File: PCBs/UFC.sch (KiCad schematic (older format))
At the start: 33 parts, among them J1 8 Pin Connector, SW1 SW_SPST, SW10 SW_SPST, SW11 SW_SPST, SW12 SW_SPST, SW13 SW_SPST, SW14 SW_SPST, SW15 SW_SPST, SW16 SW_SPST, SW17 SW_SPST, SW2 SW_SPST, SW3 SW_SPST, SW4 SW_SPST, SW5 SW_SPST, SW6 SW_SPST, SW7 SW_SPST, SW8 SW_SPST, SW9 SW_SPST, U1 STM32F103C8T6

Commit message: Split up board, started routing traces
Moved the LED drivers and the STM32 board off of the main board and onto a daughterboard to fit a reasonable space. Second board will go behind the first, connected with .1" headers. 
Additionally, traces on the bottom four (second LED driver) OPT displays are routed. 
Redid the OPT buttons to be included in the keypad matrix, to save pins.
Removed the shift register pins and wired it all directly to the STM32, to save space
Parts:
- removed A1: ShiftRegisterBoard, UFC:ShiftRegisterBoardPins, symbol UFClib:ShiftRegisterBoard
- removed C3: .1nF, Capacitor_SMD:C_0603_1608Metric_Pad1.08x0.95mm_HandSolder, symbol Device:C
- removed J1: 8 Pin Connector, UFC:8pin254mm, symbol Connector_Generic_MountingPin:Conn_01x08_MountingPin
- removed U1: STM32F103C8T6, UFC:Bluepill, symbol UFClib:STM32F103C8T6
- added D13, D14, D15, D16, D17: D, Keypad:1N4148, symbol Device:D
- added D18, D19, D20, D21, D22, D23, D24, D25, D26, D27, D28, D29, D30, D31, D32, D33, D34: LED, LED_SMD:LED_0805_2012Metric_Pad1.15x1.40mm_HandSolder, symbol Device:LED
- added DS1: Scratchpad, UFC:Scratchpad, symbol UFClib:Scratchpad
- added DS2, DS3, DS4, DS5, DS6: CustomOptPanel, UFC:OPTDisplay, symbol UFClib:CustomOptPanel
- added DS7, DS8: 14SegDisplayLumex, UFC:LDS-F3902RI, symbol UFClib:14SegDisplayLumex
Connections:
- net labels added: A1, A2, B1, B2, C1, C2, COL4, COM0-1, COM0-2, COM1-1, COM1-2, COM10-1, COM10-2, COM11-1, COM11-2, COM12-1, COM12-2, COM13-1, COM13-2, COM14-1, COM14-2, COM15-1, COM15-2, COM2-1, COM2-2, COM3-1, COM3-2, COM4-1, COM4-2, COM5-1, COM5-2, COM6-1, COM6-2, COM7-1, COM7-2, COM8-1, COM8-2, COM9-1, COM9-2, D1, D2, DOT1, DOT2, DP1, DP2, E1, E2, F1, F2, G1, G2, H1, H2, J1, J2, K1, K2, L1, L2, LEDPWM, M1, M2, N1, N2, P1, P2, Q1, Q2, ROW0
- net labels removed: CS1, CS2, DATA, RD, SRCLK, SRCS, SRMISO, SW13, SW14, SW15, SW16, SW17, WR
- wire segments 62 -> 313
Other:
- note added: "COM Channel Displays\n"
- note added: "DIG0-3 controls the halves of the two 16 segment digits\nDIG4-8 controls the 7 segment digits, 2 digits per common pin"
- note added: "Keypad LEDs\n"
- note added: "OPT button LEDs\n"
- moved on the sheet: D1, D10, D11, D12, D2, D3, D4, D5, D6, D7, D8, D9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

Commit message: Finished routing, updated comm channel displays
Decided to use (and again modify) open hornet's com channel indicators. Finished routing traces and adding ground planes on the main board, though it may be a little sloppy. Began work on the back side board, which will have the LED drivers and STM32. Re added the shift register board for now for the sake of having more pins.
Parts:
- removed DS7, DS8: 14SegDisplayLumex, UFC:LDS-F3902RI, symbol UFClib:14SegDisplayLumex
- added DS7, DS8: CommDS, UFC:OHComm, symbol UFClib:CommDS
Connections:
- wire segments 313 -> 311
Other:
- moved on the sheet: D1, D10, D11, D12, D13, D14, D15, D16, D17, D18, D19, D2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

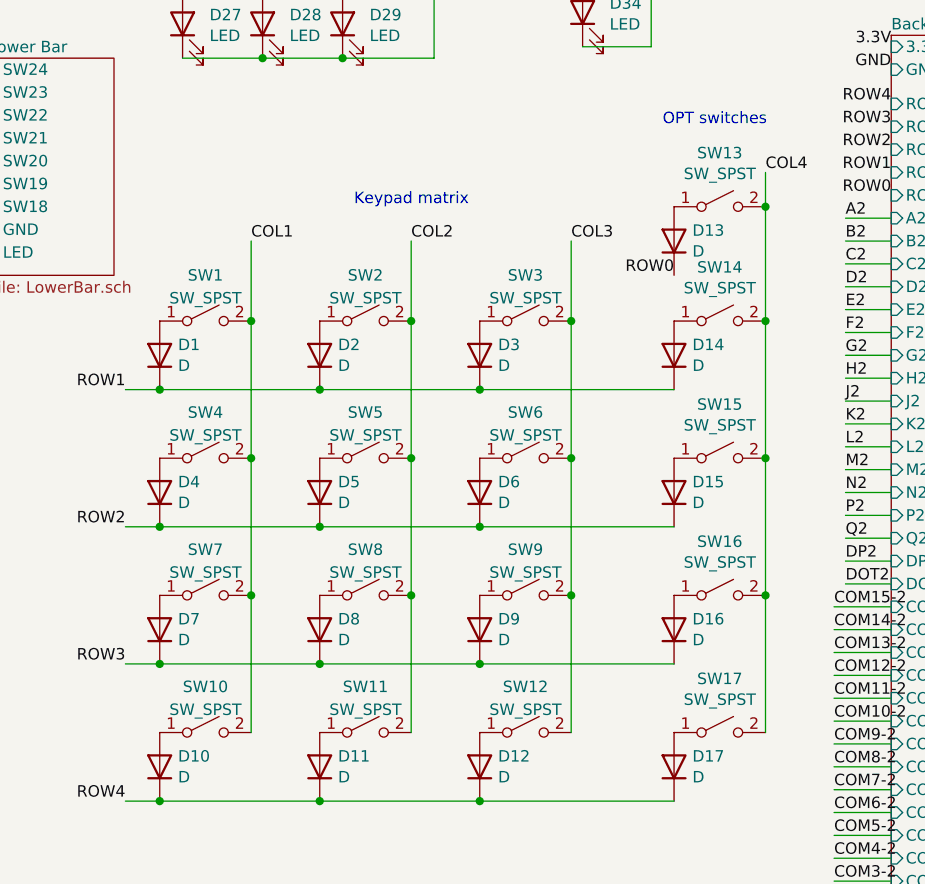
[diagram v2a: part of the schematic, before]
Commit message: Updated silkscreen, fixed minor issues
Updated silkscreen to include pin designations, and fixed minor issue with ground plane
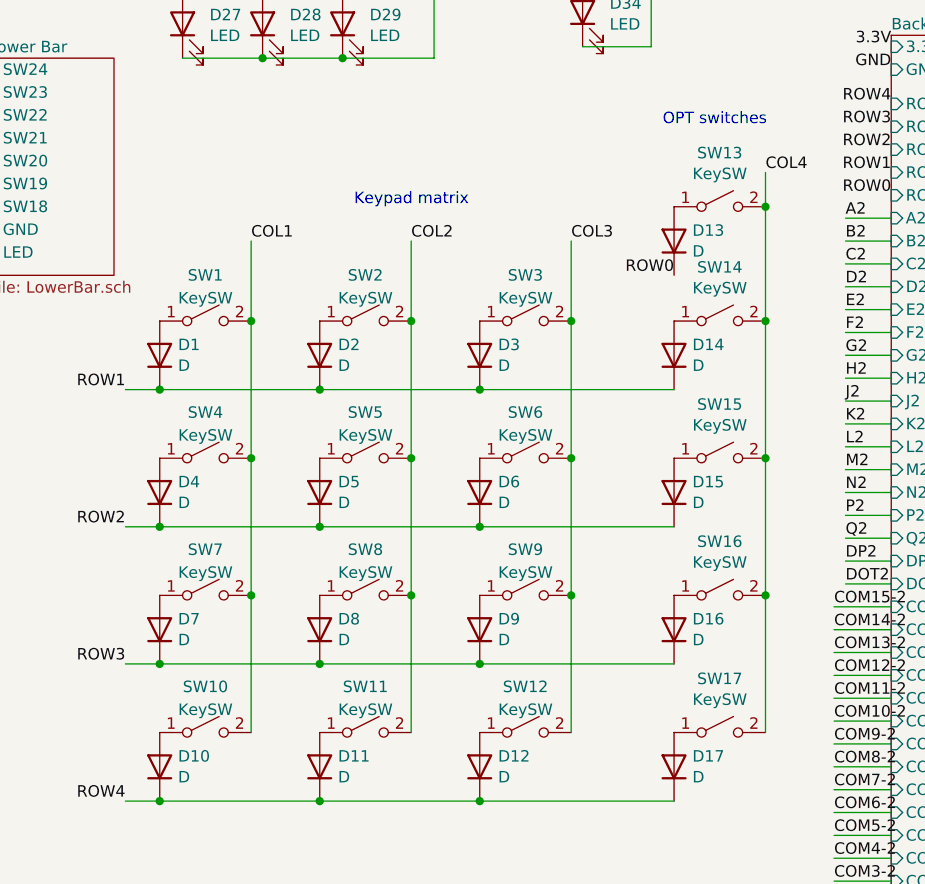
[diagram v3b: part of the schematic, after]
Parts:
- SW1, SW10, SW11, SW12, SW13, SW14, SW15, SW16, SW17, SW2, SW3, SW4, SW5, SW6, SW7, SW8, SW9: value SW_SPST -> KeySW
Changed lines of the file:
@@
 P 2200 4000
 F 0 "SW1" H 2200 4200 50  0000 C CNN
-F 1 "SW_SPST" H 2200 4100 50  0000 C CNN
+F 1 "KeySW" H 2200 4100 50  0000 C CNN
 F 2 "Keypad:KailhSW" H 2200 4000 50  0001 C CNN
 F 3 "~" H 2200 4000 50  0001 C CNN
@@
 P 2900 4000
 F 0 "SW2" H 2900 4200 50  0000 C CNN
-F 1 "SW_SPST" H 2900 4100 50  0000 C CNN
+F 1 "KeySW" H 2900 4100 50  0000 C CNN
 F 2 "Keypad:KailhSW" H 2900 4000 50  0001 C CNN
 F 3 "~" H 2900 4000 50  0001 C CNN
@@
 P 3600 4000
 F 0 "SW3" H 3600 4200 50  0000 C CNN
-F 1 "SW_SPST" H 3600 4100 50  0000 C CNN
+F 1 "KeySW" H 3600 4100 50  0000 C CNN
 F 2 "Keypad:KailhSW" H 3600 4000 50  0001 C CNN
 F 3 "~" H 3600 4000 50  0001 C CNN
@@
 P 2200 4600
 F 0 "SW4" H 2200 4800 50  0000 C CNN
-F 1 "SW_SPST" H 2200 4700 50  0000 C CNN
+F 1 "KeySW" H 2200 4700 50  0000 C CNN
 F 2 "Keypad:KailhSW" H 2200 4600 50  0001 C CNN
 F 3 "~" H 2200 4600 50  0001 C CNN
@@
 P 2900 4600
 F 0 "SW5" H 2900 4800 50  0000 C CNN
-F 1 "SW_SPST" H 2900 4700 50  0000 C CNN
+F 1 "KeySW" H 2900 4700 50  0000 C CNN
 F 2 "Keypad:KailhSW" H 2900 4600 50  0001 C CNN
 F 3 "~" H 2900 4600 50  0001 C CNN
@@
 P 3600 4600
 F 0 "SW6" H 3600 4800 50  0000 C CNN
-F 1 "SW_SPST" H 3600 4700 50  0000 C CNN
+F 1 "KeySW" H 3600 4700 50  0000 C CNN
 F 2 "Keypad:KailhSW" H 3600 4600 50  0001 C CNN
 F 3 "~" H 3600 4600 50  0001 C CNN
@@
 P 2200 5800
 F 0 "SW10" H 2200 6000 50  0000 C CNN
-F 1 "SW_SPST" H 2200 5900 50  0000 C CNN
+F 1 "KeySW" H 2200 5900 50  0000 C CNN
 F 2 "Keypad:KailhSW" H 2200 5800 50  0001 C CNN
 F 3 "~" H 2200 5800 50  0001 C CNN
@@
 P 2900 5800
 F 0 "SW11" H 2900 6000 50  0000 C CNN
-F 1 "SW_SPST" H 2900 5900 50  0000 C CNN
+F 1 "KeySW" H 2900 5900 50  0000 C CNN
 F 2 "Keypad:KailhSW" H 2900 5800 50  0001 C CNN
 F 3 "~" H 2900 5800 50  0001 C CNN
@@
 P 3600 5800
 F 0 "SW12" H 3600 6000 50  0000 C CNN
-F 1 "SW_SPST" H 3600 5900 50  0000 C CNN
+F 1 "KeySW" H 3600 5900 50  0000 C CNN
 F 2 "Keypad:KailhSW" H 3600 5800 50  0001 C CNN
 F 3 "~" H 3600 5800 50  0001 C CNN
@@
 P 3600 5200
 F 0 "SW9" H 3600 5400 50  0000 C CNN
-F 1 "SW_SPST" H 3600 5300 50  0000 C CNN
+F 1 "KeySW" H 3600 5300 50  0000 C CNN
 F 2 "Keypad:KailhSW" H 3600 5200 50  0001 C CNN
 F 3 "~" H 3600 5200 50  0001 C CNN
@@
 P 2900 5200
 F 0 "SW8" H 2900 5400 50  0000 C CNN
-F 1 "SW_SPST" H 2900 5300 50  0000 C CNN
+F 1 "KeySW" H 2900 5300 50  0000 C CNN
 F 2 "Keypad:KailhSW" H 2900 5200 50  0001 C CNN
 F 3 "~" H 2900 5200 50  0001 C CNN
@@
 P 2200 5200
 F 0 "SW7" H 2200 5400 50  0000 C CNN
-F 1 "SW_SPST" H 2200 5300 50  0000 C CNN
+F 1 "KeySW" H 2200 5300 50  0000 C CNN
 F 2 "Keypad:KailhSW" H 2200 5200 50  0001 C CNN
 F 3 "~" H 2200 5200 50  0001 C CNN
@@
 P 4450 3500
 F 0 "SW13" H 4450 3735 50  0000 C CNN
-F 1 "SW_SPST" H 4450 3644 50  0000 C CNN
+F 1 "KeySW" H 4450 3644 50  0000 C CNN
 F 2 "Keypad:KailhSW" H 4450 3500 50  0001 C CNN
 F 3 "~" H 4450 3500 50  0001 C CNN
@@
 P 4450 4000
 F 0 "SW14" H 4450 4235 50  0000 C CNN
-F 1 "SW_SPST" H 4450 4144 50  0000 C CNN
+F 1 "KeySW" H 4450 4144 50  0000 C CNN
 F 2 "Keypad:KailhSW" H 4450 4000 50  0001 C CNN
 F 3 "~" H 4450 4000 50  0001 C CNN
@@
 P 4450 4600
 F 0 "SW15" H 4450 4835 50  0000 C CNN
-F 1 "SW_SPST" H 4450 4744 50  0000 C CNN
+F 1 "KeySW" H 4450 4744 50  0000 C CNN
 F 2 "Keypad:KailhSW" H 4450 4600 50  0001 C CNN
 F 3 "~" H 4450 4600 50  0001 C CNN
@@
 P 4450 5200
 F 0 "SW16" H 4450 5435 50  0000 C CNN
-F 1 "SW_SPST" H 4450 5344 50  0000 C CNN
+F 1 "KeySW" H 4450 5344 50  0000 C CNN
 F 2 "Keypad:KailhSW" H 4450 5200 50  0001 C CNN
 F 3 "~" H 4450 5200 50  0001 C CNN
@@
 P 4450 5800
 F 0 "SW17" H 4450 6035 50  0000 C CNN
-F 1 "SW_SPST" H 4450 5944 50  0000 C CNN
+F 1 "KeySW" H 4450 5944 50  0000 C CNN
 F 2 "Keypad:KailhSW" H 4450 5800 50  0001 C CNN
 F 3 "~" H 4450 5800 50  0001 C CNN

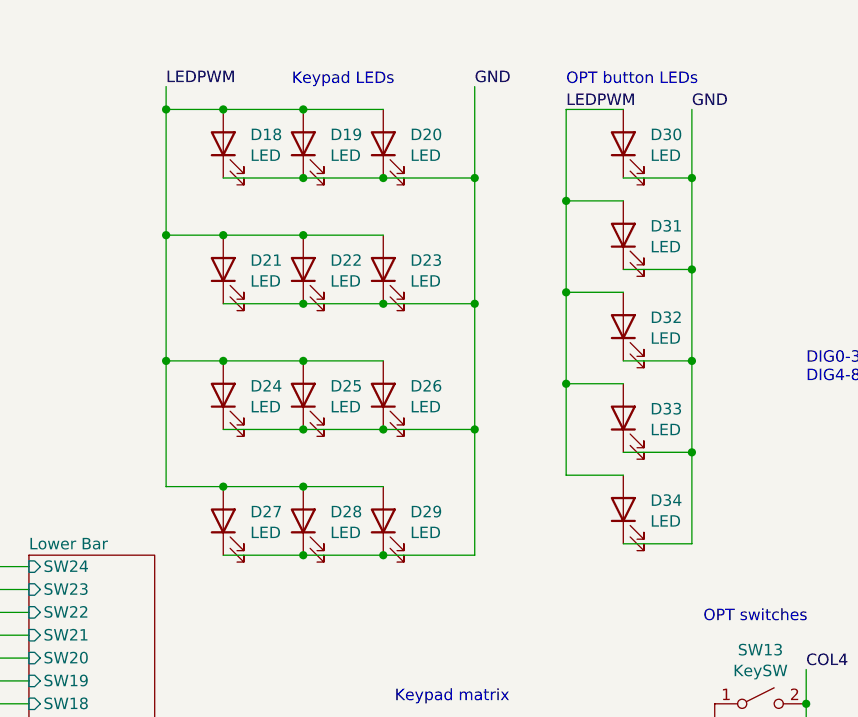
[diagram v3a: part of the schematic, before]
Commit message: Fixed design error
Untested as of now.
Removed direct connection from PWM out to LEDs, as the PWM pins on the bluepill can't provide enough current. Added P channel mosfet, and individual resistors per parallel LED. For now, the single resistor for all LEDs is still present, but bypassable via jumper, for the sake of backwards compatibility.
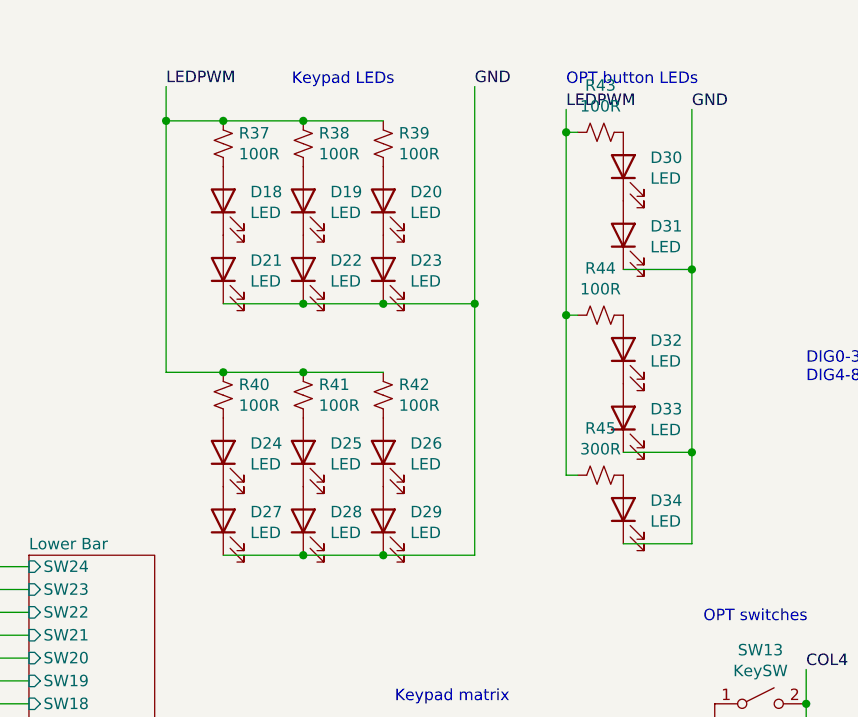
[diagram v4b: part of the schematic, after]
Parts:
- added R37, R38, R39, R40, R41, R42, R43, R44: 100R, Resistor_SMD:R_1206_3216Metric_Pad1.30x1.75mm_HandSolder, symbol Device:R_Small_US
- added R45: 300R, Resistor_SMD:R_1206_3216Metric_Pad1.30x1.75mm_HandSolder, symbol Device:R_Small_US
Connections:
- net GND: no longer D18.1 (K), D19.1 (K), D20.1 (K), D24.1 (K), D25.1 (K), D26.1 (K), D30.1 (K), D32.1 (K)
- net LEDPWM: now also R37.1, R38.1, R39.1, R40.1, R41.1, R42.1, R43.1, R44.1, R45.1; no longer D18.2 (A), D19.2 (A), D20.2 (A), D21.2 (A), D22.2 (A), D23.2 (A), D24.2 (A), D25.2 (A), D26.2 (A), D27.2 (A), D28.2 (A), D29.2 (A), D30.2 (A), D31.2 (A), D32.2 (A), D33.2 (A), D34.2 (A)
- new net: D18.1 (K), D21.2 (A)
- new net: D18.2 (A), R37.2
- new net: D19.1 (K), D22.2 (A)
- new net: D19.2 (A), R38.2
- new net: D20.1 (K), D23.2 (A)
- new net: D20.2 (A), R39.2
- new net: D24.1 (K), D27.2 (A)
- new net: D24.2 (A), R40.2
- new net: D25.1 (K), D28.2 (A)
- new net: D25.2 (A), R41.2
- new net: D26.1 (K), D29.2 (A)
- new net: D26.2 (A), R42.2
- new net: D30.1 (K), D31.2 (A)
- new net: D30.2 (A), R43.2
- new net: D32.1 (K), D33.2 (A)
- new net: D32.2 (A), R44.2
- new net: D34.2 (A), R45.2
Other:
- moved on the sheet: D18, D19, D20, D24, D25, D26, D30, D32
